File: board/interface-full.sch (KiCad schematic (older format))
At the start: 15 parts, among them J1 RASPBERRY PI, J10 RPI_RX, J11 GND, J2 From Wall Switch, J3 From Wall Switch, J4 From Wall Switch, J5 To Relay, J6 To Relay, J7 To Relay, J8 RPI_TX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

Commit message: firmware changes to support toggle and momentary swithces. I have no idea what was the hardware modifications
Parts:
- C1: symbol Device:CP -> interface-full-rescue:CP-Device
- C2: symbol Device:C_Small -> interface-full-rescue:C_Small-Device
- D1: symbol Device:LED_ALT -> interface-full-rescue:LED_ALT-Device
- J1: symbol Connector_Generic:Conn_02x20_Odd_Even -> interface-full-rescue:Conn_02x20_Odd_Even-Connector_Generic
- J10, J11, J8: symbol Connector_Generic:Conn_01x01 -> interface-full-rescue:Conn_01x01-Connector_Generic
- J2, J3, J4, J5, J6, J7: symbol Connector:Screw_Terminal_01x04 -> interface-full-rescue:Screw_Terminal_01x04-Connector
- J9: symbol Connector:Screw_Terminal_01x02 -> interface-full-rescue:Screw_Terminal_01x02-Connector
- R1: symbol Device:R -> interface-full-rescue:R-Device
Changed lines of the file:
@@
 $EndDescr
 $Comp
-L Connector_Generic:Conn_02x20_Odd_Even J1
+L interface-full-rescue:Conn_02x20_Odd_Even-Connector_Generic J1
 U 1 1 5E337FEB
 P 1800 1800
@@
 	2450 2400 2100 2400
 $Comp
-L Connector:Screw_Terminal_01x02 J9
+L interface-full-rescue:Screw_Terminal_01x02-Connector J9
 U 1 1 5E34AE0F
 P 3450 7100
@@
 	3650 7100 3750 7100
 $Comp
-L power:+5V #PWR02
+L interface-full-rescue:+5V-power #PWR02
 U 1 1 5E34E075
 P 3750 6950
@@
 $EndComp
 $Comp
-L power:GND #PWR05
+L interface-full-rescue:GND-power #PWR05
 U 1 1 5E34ED7B
 P 3750 7350
@@
 $EndSheet
 $Comp
-L Device:C_Small C2
+L interface-full-rescue:C_Small-Device C2
 U 1 1 5E34A4DA
 P 6450 7150
@@
 $EndComp
 $Comp
-L power:+5V #PWR04
+L interface-full-rescue:+5V-power #PWR04
 U 1 1 5E34A4E0
 P 6450 7000
@@
 $EndComp
 $Comp
-L power:GND #PWR08
+L interface-full-rescue:GND-power #PWR08
 U 1 1 5E34A4E6
 P 6450 7350
@@
 $EndComp
 $Comp
-L Device:CP C1
+L interface-full-rescue:CP-Device C1
 U 1 1 5E34A4EC
 P 6050 7150
@@
 $EndComp
 $Comp
-L power:+5V #PWR03
+L interface-full-rescue:+5V-power #PWR03
 U 1 1 5E34A4F2
 P 6050 7000
@@
 $EndComp
 $Comp
-L power:GND #PWR07
+L interface-full-rescue:GND-power #PWR07
 U 1 1 5E34A4F8
 P 6050 7350
@@
 	6050 7300 6050 7350
 $Comp
-L Device:LED_ALT D1
+L interface-full-rescue:LED_ALT-Device D1
 U 1 1 5E34A4FF
 P 5450 7150
@@
 $EndComp
 $Comp
-L Device:R R1
+L interface-full-rescue:R-Device R1
 U 1 1 5E34A505
 P 5450 6800
@@
 $EndComp
 $Comp
-L power:GND #PWR06
+L interface-full-rescue:GND-power #PWR06
 U 1 1 5E34A50B
 P 5450 7350
@@
 	5450 7000 5450 6950
 $Comp
-L power:+5V #PWR01
+L interface-full-rescue:+5V-power #PWR01
 U 1 1 5E34A512
 P 5450 6600
@@
 $EndSheet
 $Comp
-L power:PWR_FLAG #FLG01
+L interface-full-rescue:PWR_FLAG-power #FLG01
 U 1 1 5E38365D
 P 4100 6950
@@
 $EndComp
 $Comp
-L power:PWR_FLAG #FLG02
+L interface-full-rescue:PWR_FLAG-power #FLG02
 U 1 1 5E383B3D
 P 4100 7350
@@
 	6450 7250 6450 7350
 $Comp
-L Connector:Screw_Terminal_01x04 J2
+L interface-full-rescue:Screw_Terminal_01x04-Connector J2
 U 1 1 5E3B48A5
 P 3850 4250
@@
 $EndComp
 $Comp
-L Connector:Screw_Terminal_01x04 J3
+L interface-full-rescue:Screw_Terminal_01x04-Connector J3
 U 1 1 5E3B65C8
 P 6400 4300
@@
 $EndComp
 $Comp
-L Connector:Screw_Terminal_01x04 J6
+L interface-full-rescue:Screw_Terminal_01x04-Connector J6
 U 1 1 5E3B733E
 P 6400 5200
@@
 $EndComp
 $Comp
-L Connector:Screw_Terminal_01x04 J4
+L interface-full-rescue:Screw_Terminal_01x04-Connector J4
 U 1 1 5E3B7813
 P 8950 4300
@@
 $EndComp
 $Comp
-L Connector:Screw_Terminal_01x04 J7
+L interface-full-rescue:Screw_Terminal_01x04-Connector J7
 U 1 1 5E3B83CF
 P 8950 5200
@@
 $EndComp
 $Comp
-L Connector:Screw_Terminal_01x04 J5
+L interface-full-rescue:Screw_Terminal_01x04-Connector J5
 U 1 1 5E3B5C3C
 P 3850 5150
@@
 	1700 7200 1850 7200
 $Comp
-L power:GND #PWR09
+L interface-full-rescue:GND-power #PWR09
 U 1 1 5E429319
 P 1850 7450
@@
 	1850 7300 1700 7300
 $Comp
-L Connector_Generic:Conn_01x01 J?
+L interface-full-rescue:Conn_01x01-Connector_Generic J?
 U 1 1 5E40F2AF
 P 1500 7300
@@
 $EndComp
 $Comp
-L Connector_Generic:Conn_01x01 J?
+L interface-full-rescue:Conn_01x01-Connector_Generic J?
 U 1 1 5E40F2A9
 P 1500 7100
@@
 $EndComp
 $Comp
-L Connector_Generic:Conn_01x01 J?
+L interface-full-rescue:Conn_01x01-Connector_Generic J?
 U 1 1 5E40F2A3
 P 1500 7200

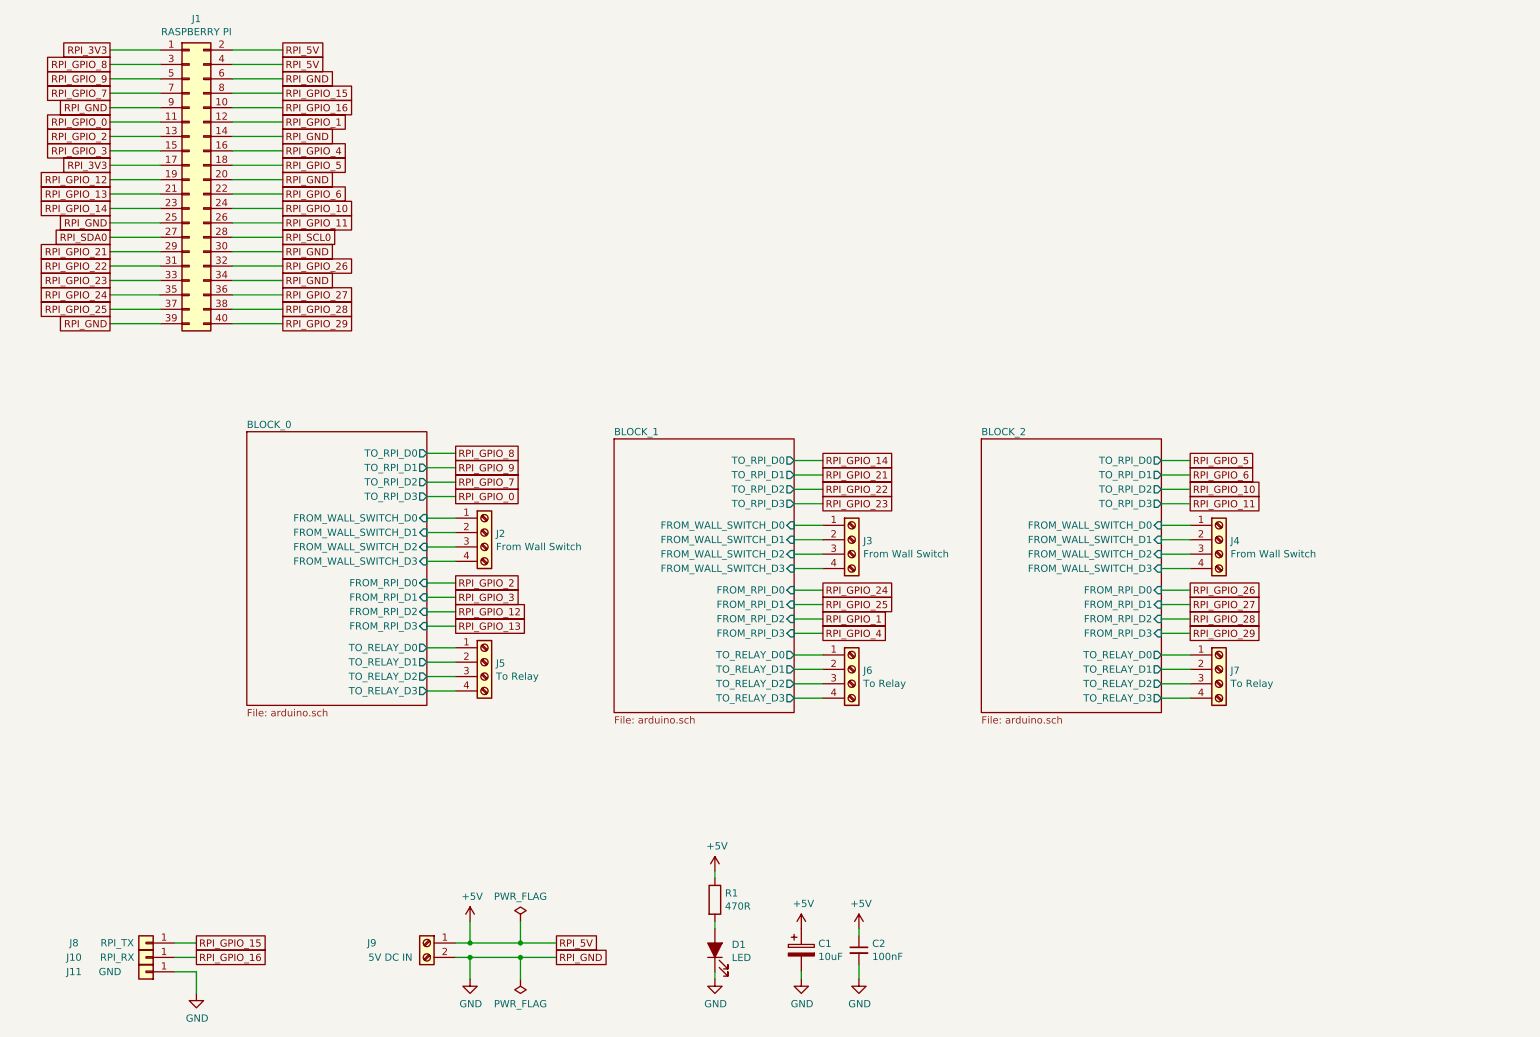
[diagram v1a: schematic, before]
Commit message: change sch to match rpi gpio numbering
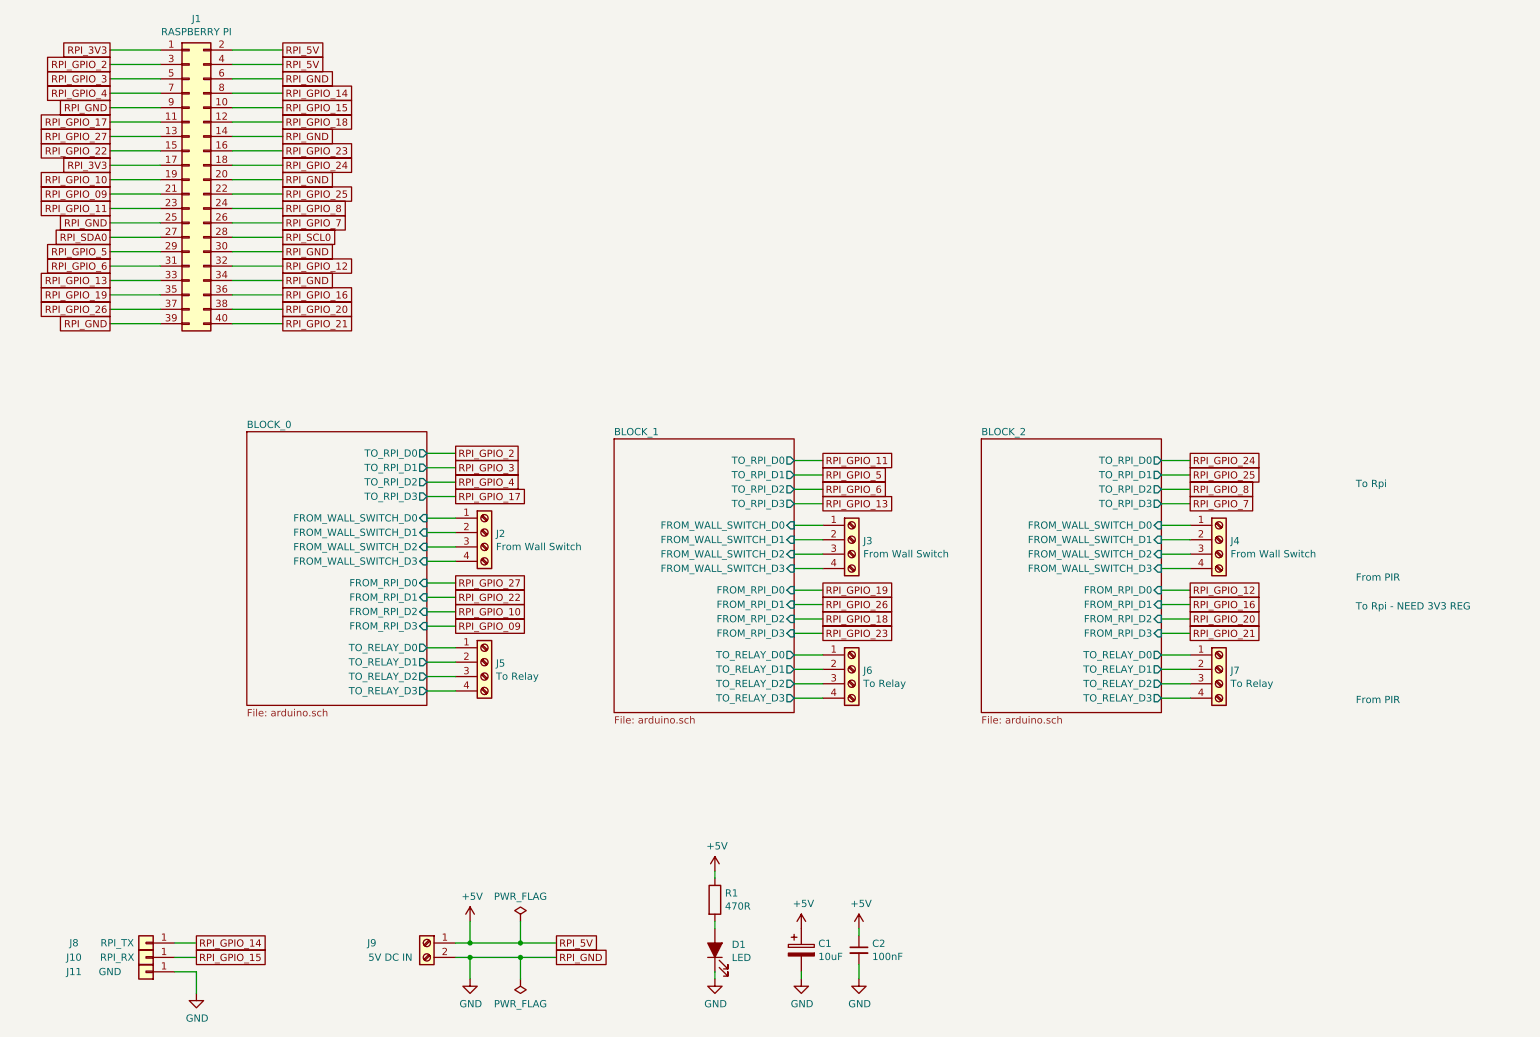
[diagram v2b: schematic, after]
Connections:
- net RPI_GPIO_29 is gone; now on net RPI_GPIO_21: J1.40 (Pin_40)
- net RPI_GPIO_9 is gone; now on net RPI_GPIO_3: J1.5 (Pin_5)
- net RPI_GPIO_10: now also J1.19 (Pin_19); no longer J1.24 (Pin_24)
- net RPI_GPIO_11: now also J1.23 (Pin_23); no longer J1.26 (Pin_26)
- net RPI_GPIO_12: now also J1.32 (Pin_32); no longer J1.19 (Pin_19)
- net RPI_GPIO_13: now also J1.33 (Pin_33); no longer J1.21 (Pin_21)
- net RPI_GPIO_14: now also J1.8 (Pin_8), J8.1 (Pin_1); no longer J1.23 (Pin_23)
- net RPI_GPIO_15: now also J1.10 (Pin_10), J10.1 (Pin_1); no longer J1.8 (Pin_8), J8.1 (Pin_1)
- net RPI_GPIO_16: now also J1.36 (Pin_36); no longer J1.10 (Pin_10), J10.1 (Pin_1)
- net RPI_GPIO_2: now also J1.3 (Pin_3); no longer J1.13 (Pin_13)
- net RPI_GPIO_21: no longer J1.29 (Pin_29)
- net RPI_GPIO_22: now also J1.15 (Pin_15); no longer J1.31 (Pin_31)
- net RPI_GPIO_23: now also J1.16 (Pin_16); no longer J1.33 (Pin_33)
- net RPI_GPIO_24: now also J1.18 (Pin_18); no longer J1.35 (Pin_35)
- net RPI_GPIO_25: now also J1.22 (Pin_22); no longer J1.37 (Pin_37)
- net RPI_GPIO_26: now also J1.37 (Pin_37); no longer J1.32 (Pin_32)
- net RPI_GPIO_27: now also J1.13 (Pin_13); no longer J1.36 (Pin_36)
- net RPI_GPIO_3: no longer J1.15 (Pin_15)
- net RPI_GPIO_4: now also J1.7 (Pin_7); no longer J1.16 (Pin_16)
- net RPI_GPIO_5: now also J1.29 (Pin_29); no longer J1.18 (Pin_18)
- net RPI_GPIO_6: now also J1.31 (Pin_31); no longer J1.22 (Pin_22)
- net RPI_GPIO_7: now also J1.26 (Pin_26); no longer J1.7 (Pin_7)
- net RPI_GPIO_8: now also J1.24 (Pin_24); no longer J1.3 (Pin_3)
- net RPI_GPIO_0 renamed RPI_GPIO_17
- net RPI_GPIO_1 renamed RPI_GPIO_18
- net RPI_GPIO_28 renamed RPI_GPIO_20
- new net RPI_GPIO_09: J1.21 (Pin_21)
- new net RPI_GPIO_19: J1.35 (Pin_35)
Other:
- note added: "From PIR"
- note added: "To Rpi"
- note added: "To Rpi - NEED 3V3 REG\n"
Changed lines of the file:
@@
 RPI_GND
 Text GLabel 2450 1200 2    50   UnSpc ~ 0
+RPI_GPIO_14
+Text GLabel 2450 1300 2    50   UnSpc ~ 0
 RPI_GPIO_15
-Text GLabel 2450 1300 2    50   UnSpc ~ 0
-RPI_GPIO_16
 Text GLabel 2450 1400 2    50   UnSpc ~ 0
-RPI_GPIO_1
+RPI_GPIO_18
 Text GLabel 2450 1500 2    50   UnSpc ~ 0
 RPI_GND
 Text GLabel 2450 1600 2    50   UnSpc ~ 0
-RPI_GPIO_4
+RPI_GPIO_23
 Text GLabel 2450 1700 2    50   UnSpc ~ 0
-RPI_GPIO_5
+RPI_GPIO_24
 Text GLabel 2450 1800 2    50   UnSpc ~ 0
 RPI_GND
 Text GLabel 2450 1900 2    50   UnSpc ~ 0
-RPI_GPIO_6
+RPI_GPIO_25
 Text GLabel 2450 2000 2    50   UnSpc ~ 0
-RPI_GPIO_10
+RPI_GPIO_8
 Text GLabel 2450 2100 2    50   UnSpc ~ 0
-RPI_GPIO_11
+RPI_GPIO_7
 Text GLabel 2450 2200 2    50   UnSpc ~ 0
 RPI_SCL0
@@
 RPI_GND
 Text GLabel 2450 2400 2    50   UnSpc ~ 0
+RPI_GPIO_12
+Text GLabel 2450 2500 2    50   UnSpc ~ 0
+RPI_GND
+Text GLabel 2450 2600 2    50   UnSpc ~ 0
+RPI_GPIO_16
+Text GLabel 2450 2700 2    50   UnSpc ~ 0
+RPI_GPIO_20
+Text GLabel 2450 2800 2    50   UnSpc ~ 0
+RPI_GPIO_21
+Text GLabel 1250 2800 0    50   UnSpc ~ 0
+RPI_GND
+Text GLabel 1250 2700 0    50   UnSpc ~ 0
 RPI_GPIO_26
-Text GLabel 2450 2500 2    50   UnSpc ~ 0
-RPI_GND
-Text GLabel 2450 2600 2    50   UnSpc ~ 0
-RPI_GPIO_27
-Text GLabel 2450 2700 2    50   UnSpc ~ 0
-RPI_GPIO_28
-Text GLabel 2450 2800 2    50   UnSpc ~ 0
-RPI_GPIO_29
-Text GLabel 1250 2800 0    50   UnSpc ~ 0
-RPI_GND
-Text GLabel 1250 2700 0    50   UnSpc ~ 0
-RPI_GPIO_25
 Text GLabel 1250 2600 0    50   UnSpc ~ 0
-RPI_GPIO_24
+RPI_GPIO_19
 Text GLabel 1250 2500 0    50   UnSpc ~ 0
-RPI_GPIO_23
+RPI_GPIO_13
 Text GLabel 1250 2400 0    50   UnSpc ~ 0
-RPI_GPIO_22
+RPI_GPIO_6
 Text GLabel 1250 2300 0    50   UnSpc ~ 0
-RPI_GPIO_21
+RPI_GPIO_5
 Text GLabel 1250 2200 0    50   UnSpc ~ 0
 RPI_SDA0
@@
 RPI_GND
 Text GLabel 1250 2000 0    50   UnSpc ~ 0
-RPI_GPIO_14
+RPI_GPIO_11
 Text GLabel 1250 1900 0    50   UnSpc ~ 0
-RPI_GPIO_13
+RPI_GPIO_09
 Text GLabel 1250 1800 0    50   UnSpc ~ 0
-RPI_GPIO_12
+RPI_GPIO_10
 Text GLabel 1250 1700 0    50   UnSpc ~ 0
 RPI_3V3
 Text GLabel 1250 1200 0    50   UnSpc ~ 0
-RPI_GPIO_7
+RPI_GPIO_4
 Text GLabel 1250 1300 0    50   UnSpc ~ 0
 RPI_GND
 Text GLabel 1250 1400 0    50   UnSpc ~ 0
-RPI_GPIO_0
+RPI_GPIO_17
 Text GLabel 1250 1500 0    50   UnSpc ~ 0
+RPI_GPIO_27
+Text GLabel 1250 1600 0    50   UnSpc ~ 0
+RPI_GPIO_22
+Text GLabel 1250 1100 0    50   UnSpc ~ 0
+RPI_GPIO_3
+Text GLabel 1250 1000 0    50   UnSpc ~ 0
 RPI_GPIO_2
-Text GLabel 1250 1600 0    50   UnSpc ~ 0
-RPI_GPIO_3
-Text GLabel 1250 1100 0    50   UnSpc ~ 0
-RPI_GPIO_9
-Text GLabel 1250 1000 0    50   UnSpc ~ 0
-RPI_GPIO_8
 Text GLabel 1250 900  0    50   UnSpc ~ 0
 RPI_3V3
@@
 	4100 7350 4100 7200
 Text GLabel 6200 4750 2    50   UnSpc ~ 0
+RPI_GPIO_26
+Text GLabel 6200 4650 2    50   UnSpc ~ 0
+RPI_GPIO_19
+Text GLabel 6200 4050 2    50   UnSpc ~ 0
+RPI_GPIO_13
+Text GLabel 6200 3950 2    50   UnSpc ~ 0
+RPI_GPIO_6
+Text GLabel 6200 3850 2    50   UnSpc ~ 0
+RPI_GPIO_5
+Text GLabel 3650 4900 2    50   UnSpc ~ 0
+RPI_GPIO_09
+Text GLabel 3650 4800 2    50   UnSpc ~ 0
+RPI_GPIO_10
+Text GLabel 3650 3900 2    50   UnSpc ~ 0
+RPI_GPIO_4
+Text GLabel 3650 4000 2    50   UnSpc ~ 0
+RPI_GPIO_17
+Text GLabel 3650 4600 2    50   UnSpc ~ 0
+RPI_GPIO_27
+Text GLabel 3650 4700 2    50   UnSpc ~ 0
+RPI_GPIO_22
+Text GLabel 3650 3800 2    50   UnSpc ~ 0
+RPI_GPIO_3
+Text GLabel 3650 3700 2    50   UnSpc ~ 0
+RPI_GPIO_2
+Text GLabel 6200 4850 2    50   UnSpc ~ 0
+RPI_GPIO_18
+Text GLabel 6200 4950 2    50   UnSpc ~ 0
+RPI_GPIO_23
+Text GLabel 8750 3750 2    50   UnSpc ~ 0
+RPI_GPIO_24
+Text GLabel 8750 3850 2    50   UnSpc ~ 0
 RPI_GPIO_25
-Text GLabel 6200 4650 2    50   UnSpc ~ 0
-RPI_GPIO_24
-Text GLabel 6200 4050 2    50   UnSpc ~ 0
-RPI_GPIO_23
-Text GLabel 6200 3950 2    50   UnSpc ~ 0
-RPI_GPIO_22
-Text GLabel 6200 3850 2    50   UnSpc ~ 0
+Text GLabel 8750 3950 2    50   UnSpc ~ 0
+RPI_GPIO_8
+Text GLabel 8750 4050 2    50   UnSpc ~ 0
+RPI_GPIO_7
+Text GLabel 8750 4650 2    50   UnSpc ~ 0
+RPI_GPIO_12
+Text GLabel 8750 4750 2    50   UnSpc ~ 0
+RPI_GPIO_16
+Text GLabel 8750 4850 2    50   UnSpc ~ 0
+RPI_GPIO_20
+Text GLabel 8750 4950 2    50   UnSpc ~ 0
 RPI_GPIO_21
-Text GLabel 3650 4900 2    50   UnSpc ~ 0
-RPI_GPIO_13
-Text GLabel 3650 4800 2    50   UnSpc ~ 0
-RPI_GPIO_12
-Text GLabel 3650 3900 2    50   UnSpc ~ 0
-RPI_GPIO_7
-Text GLabel 3650 4000 2    50   UnSpc ~ 0
-RPI_GPIO_0
-Text GLabel 3650 4600 2    50   UnSpc ~ 0
-RPI_GPIO_2
-Text GLabel 3650 4700 2    50   UnSpc ~ 0
-RPI_GPIO_3
-Text GLabel 3650 3800 2    50   UnSpc ~ 0
-RPI_GPIO_9
-Text GLabel 3650 3700 2    50   UnSpc ~ 0
-RPI_GPIO_8
-Text GLabel 6200 4850 2    50   UnSpc ~ 0
-RPI_GPIO_1
-Text GLabel 6200 4950 2    50   UnSpc ~ 0
-RPI_GPIO_4
-Text GLabel 8750 3750 2    50   UnSpc ~ 0
-RPI_GPIO_5
-Text GLabel 8750 3850 2    50   UnSpc ~ 0
-RPI_GPIO_6
-Text GLabel 8750 3950 2    50   UnSpc ~ 0
-RPI_GPIO_10
-Text GLabel 8750 4050 2    50   UnSpc ~ 0
-RPI_GPIO_11
-Text GLabel 8750 4650 2    50   UnSpc ~ 0
-RPI_GPIO_26
-Text GLabel 8750 4750 2    50   UnSpc ~ 0
-RPI_GPIO_27
-Text GLabel 8750 4850 2    50   UnSpc ~ 0
-RPI_GPIO_28
-Text GLabel 8750 4950 2    50   UnSpc ~ 0
-RPI_GPIO_29
 Connection ~ 4100 7200
 Wire Wire Line
@@
 	8550 5400 8750 5400
 Text GLabel 6200 3750 2    50   UnSpc ~ 0
+RPI_GPIO_11
+Text GLabel 1850 7200 2    50   UnSpc ~ 0
+RPI_GPIO_15
+Text GLabel 1850 7100 2    50   UnSpc ~ 0
 RPI_GPIO_14
-Text GLabel 1850 7200 2    50   UnSpc ~ 0
-RPI_GPIO_16
-Text GLabel 1850 7100 2    50   UnSpc ~ 0
-RPI_GPIO_15
 Wire Wire Line
 	1700 7100 1850 7100
@@
 	-1   0    0    1
 $EndComp
+Text Notes 9900 4600 0    50   ~ 0
+From PIR
+Text Notes 9900 5450 0    50   ~ 0
+From PIR
+Text Notes 9900 3950 0    50   ~ 0
+To Rpi
+Text Notes 9900 4800 0    50   ~ 0
+To Rpi - NEED 3V3 REG\n
 $EndSCHEMATC

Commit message: Fix RPI GPIO numbers
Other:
- note added: "For PIR Sensors, don't connect "To Relay" and "From RPI". Use "switch mode" firmware."
- note added: "NOTES:"
- note removed: "From PIR"
- note removed: "To Rpi"
- note removed: "To Rpi - NEED 3V3 REG\n"
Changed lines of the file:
@@
 	-1   0    0    1
 $EndComp
-Text Notes 9900 4600 0    50   ~ 0
-From PIR
-Text Notes 9900 5450 0    50   ~ 0
-From PIR
-Text Notes 9900 3950 0    50   ~ 0
-To Rpi
-Text Notes 9900 4800 0    50   ~ 0
-To Rpi - NEED 3V3 REG\n
+Text Notes 7000 6500 0    50   ~ 0
+For PIR Sensors, don't connect "To Relay" and "From RPI". Use "switch mode" firmware.
+Text Notes 7000 6400 0    50   ~ 0
+NOTES:
 $EndSCHEMATC
